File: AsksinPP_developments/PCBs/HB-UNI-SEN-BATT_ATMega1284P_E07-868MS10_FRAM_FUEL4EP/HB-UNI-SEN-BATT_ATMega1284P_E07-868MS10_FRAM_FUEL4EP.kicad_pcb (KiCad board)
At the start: 2 copper layers, 75 x 75 mm, 63 parts, among them J1 Conn_01x02, J10 charge, J11 ePaper connector, J12 FTDI Debuger, J13 BME680, J2 Conn_01x02, J3 Conn_01x02, J4 Conn_01x02, J5 ISP Programmer, J6 SHT85, J7 AHT25, J8 AHT20+BMP280, J9 BME280/BMP280, Q1 IRLU024N, SW1 Config button, SW2 Reset button, U1 ATmega1284P-AU, U2 TPS61221DCK, U3 MB85RS2MTPF, U4 MB85RS2MTPF, Y1 8MHz

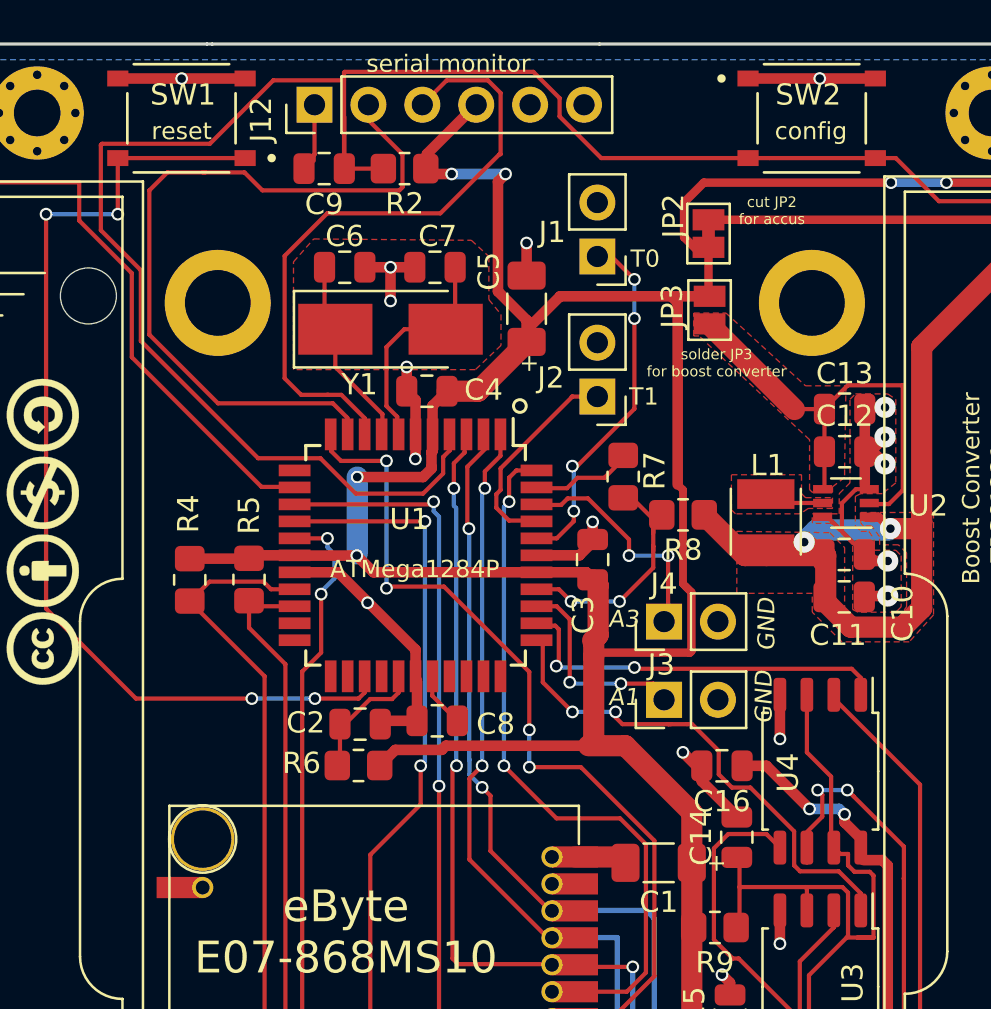
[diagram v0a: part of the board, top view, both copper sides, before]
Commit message: PCBs/HB-UNI-SEN-BATT_ATMega1284P_E07-868MS10_FUEL4EP and PCBs/HB-UNI-SEN-BATT_ATMega1284P_E07-868MS10_FRAM_FUEL4EP: changed R8 from 200kOhm to 47kOhm for better measurement accuracy
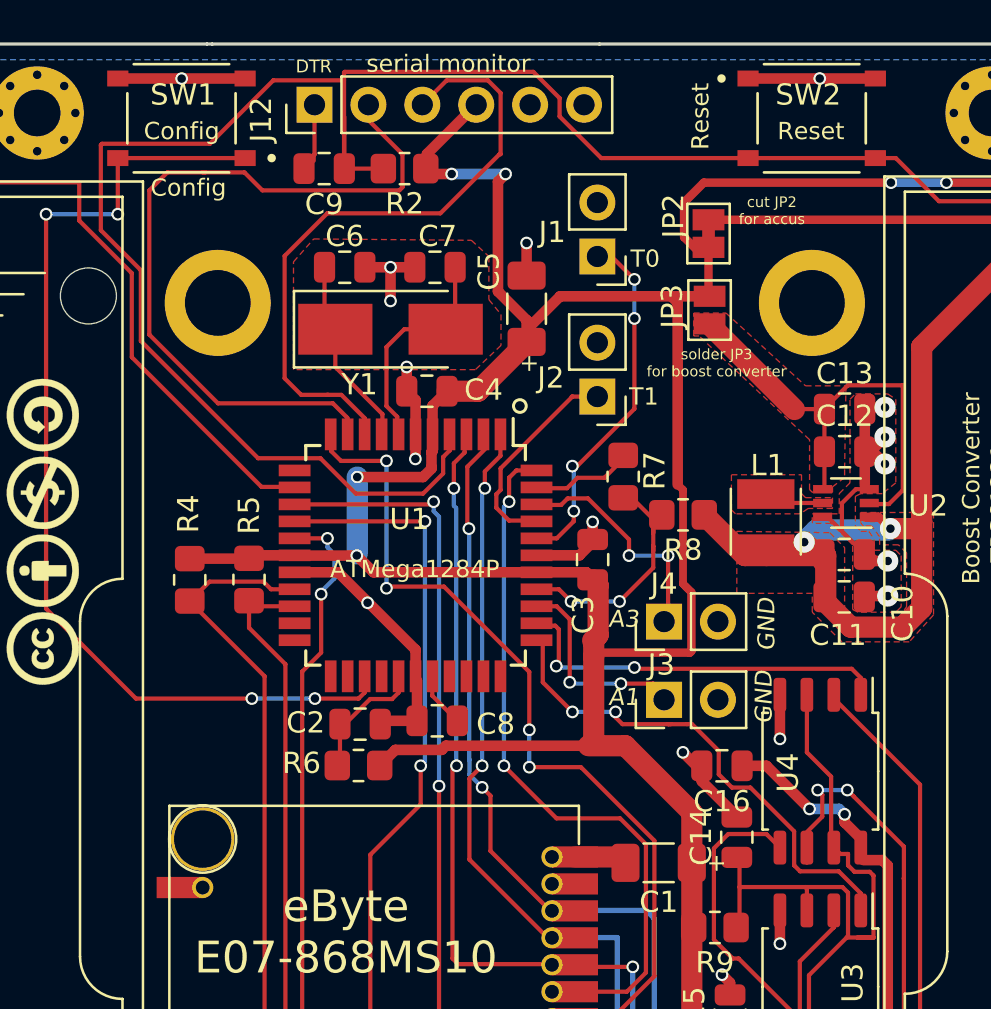
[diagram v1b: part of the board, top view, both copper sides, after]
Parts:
- R8: value 200k -> 47k
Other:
- board text added: "Config"
- board text added: "DTR"
- board text added: "Reset"
- board text added: "Version 1.1 - 01/2022"
- board text removed: "Version 1.0 - 11/2021"
- board text removed: "config"
- board text removed: "reset"

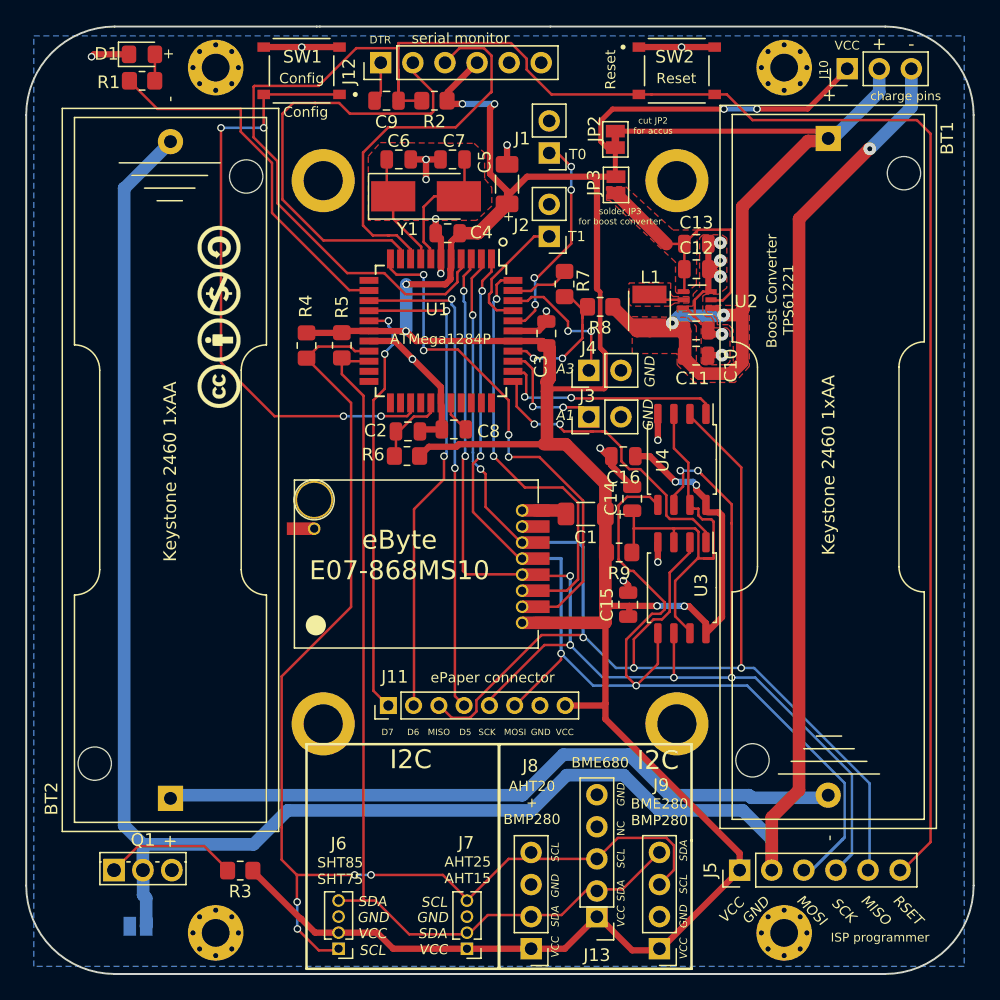
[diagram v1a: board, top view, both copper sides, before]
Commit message: major update: hb-ep-devices-addon V1.14; added sketches HB-UNI-Sensor1-AQ-BME680_KF_rLF and HB-UNI-SenAct-4-4-SC_DS; migration of all PPCBs to KiCAD 6
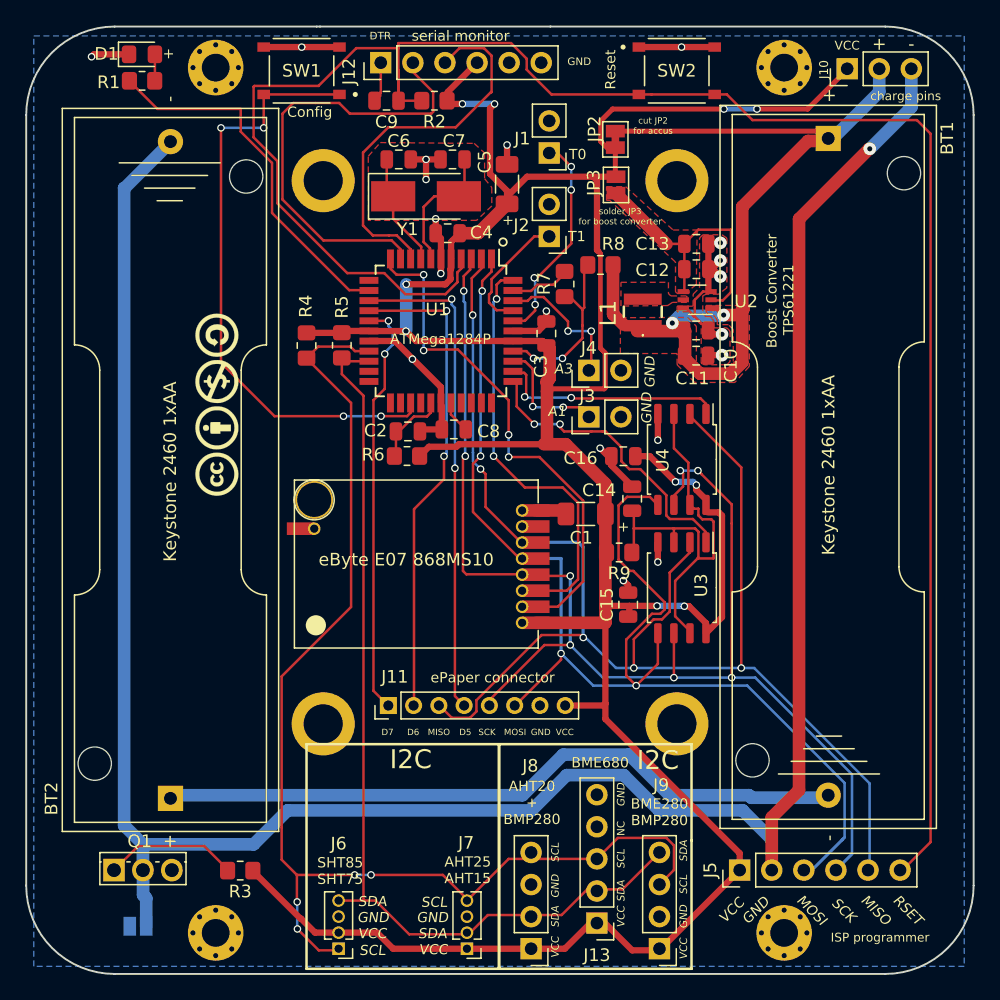
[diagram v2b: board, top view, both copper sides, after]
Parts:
- L1: footprint FUEL4EP:Fastron L-1212FPS 4.7uH SMD Inductor -> FUEL4EP:FUEL4EP_Inductor_SMD_1
- moved LOGO1 6.95 mm to (116.1, 108.0)
- moved R8 3.31 mm to (146.5, 96.9)
- moved L1 1.79 mm to (149.8, 100.6)
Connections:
- net /~hold renamed /~{hold}
- J13 pad 4: Net-(J13-Pad4) -> unconnected-(J13-Pad4)
- Module1 pad 2A: Net-(Module1-Pad2A) -> unconnected-(Module1-Pad2A)
- Module1 pad 7C: Net-(Module1-Pad7C) -> unconnected-(Module1-Pad7C)
- U1 pad 12: Net-(U1-Pad12) -> unconnected-(U1-Pad12)
- U1 pad 21: Net-(U1-Pad21) -> unconnected-(U1-Pad21)
- U1 pad 22: Net-(U1-Pad22) -> unconnected-(U1-Pad22)
- U1 pad 23: Net-(U1-Pad23) -> unconnected-(U1-Pad23)
- U1 pad 24: Net-(U1-Pad24) -> unconnected-(U1-Pad24)
- U1 pad 26: Net-(U1-Pad26) -> unconnected-(U1-Pad26)
- U1 pad 30: Net-(U1-Pad30) -> unconnected-(U1-Pad30)
- U1 pad 31: Net-(U1-Pad31) -> unconnected-(U1-Pad31)
- U1 pad 32: Net-(U1-Pad32) -> unconnected-(U1-Pad32)
- U1 pad 33: Net-(U1-Pad33) -> unconnected-(U1-Pad33)
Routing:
- net VCC: track 254.6 -> 251.4 mm
- net Net-(L1-Pad2): track 2.67 -> 0.00 mm
- net /plusBAT: track 69.9 -> 72.4 mm
- net /A0: track 12.1 -> 14.0 mm
- net /PA3: track 24.3 -> 22.9 mm
- net /~{hold}: track 33.1 -> 32.4 mm
- net /minusBAT: track 189.6 -> 189.0 mm
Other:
- net class Default removed
- net class battery removed
- net class supply removed
- board text added: "Version 1.2 - 07/2023 (KiCAD 6)"
- board text removed: "Version 1.1 - 01/2022"
- board text removed: "eByte E07-868MS10"

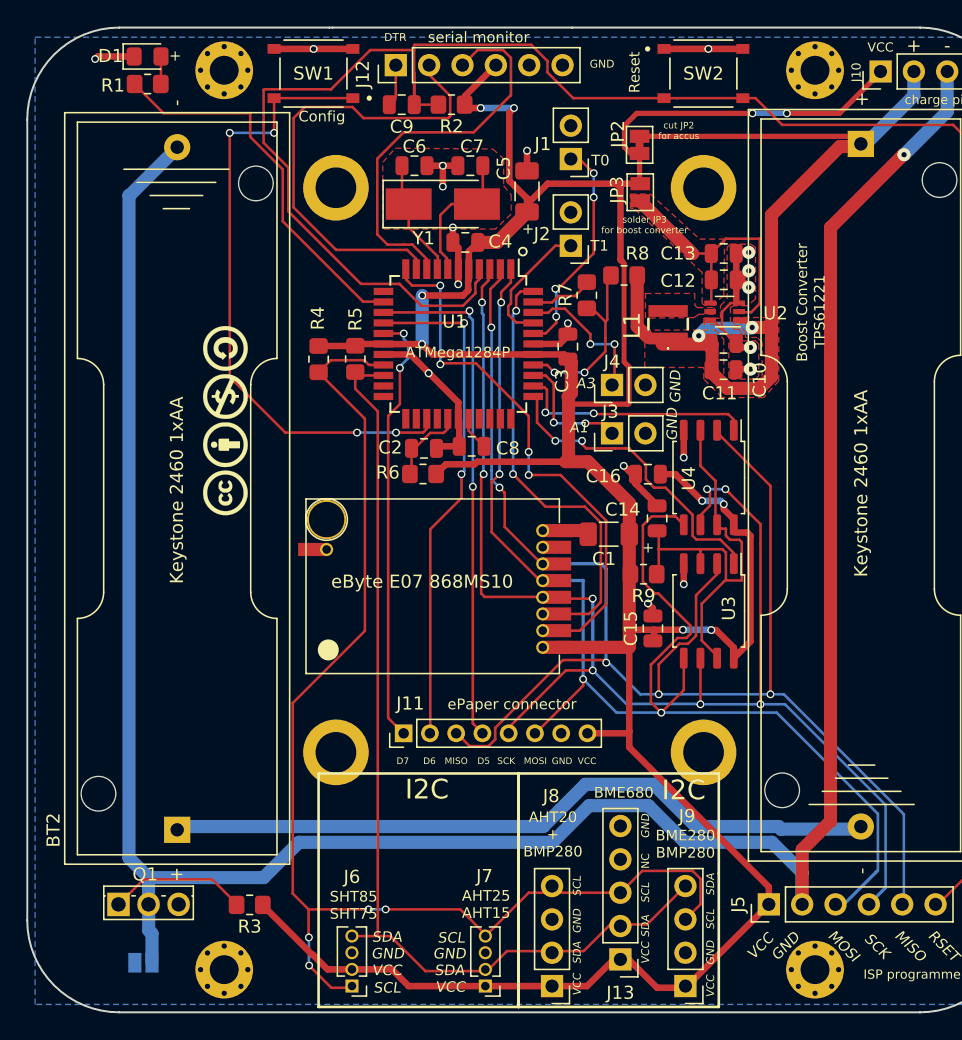
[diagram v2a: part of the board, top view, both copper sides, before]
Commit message: PCBs: KiCAD6 required improvements of layout data bases; added E07-900M10S into FUEL and footprint library
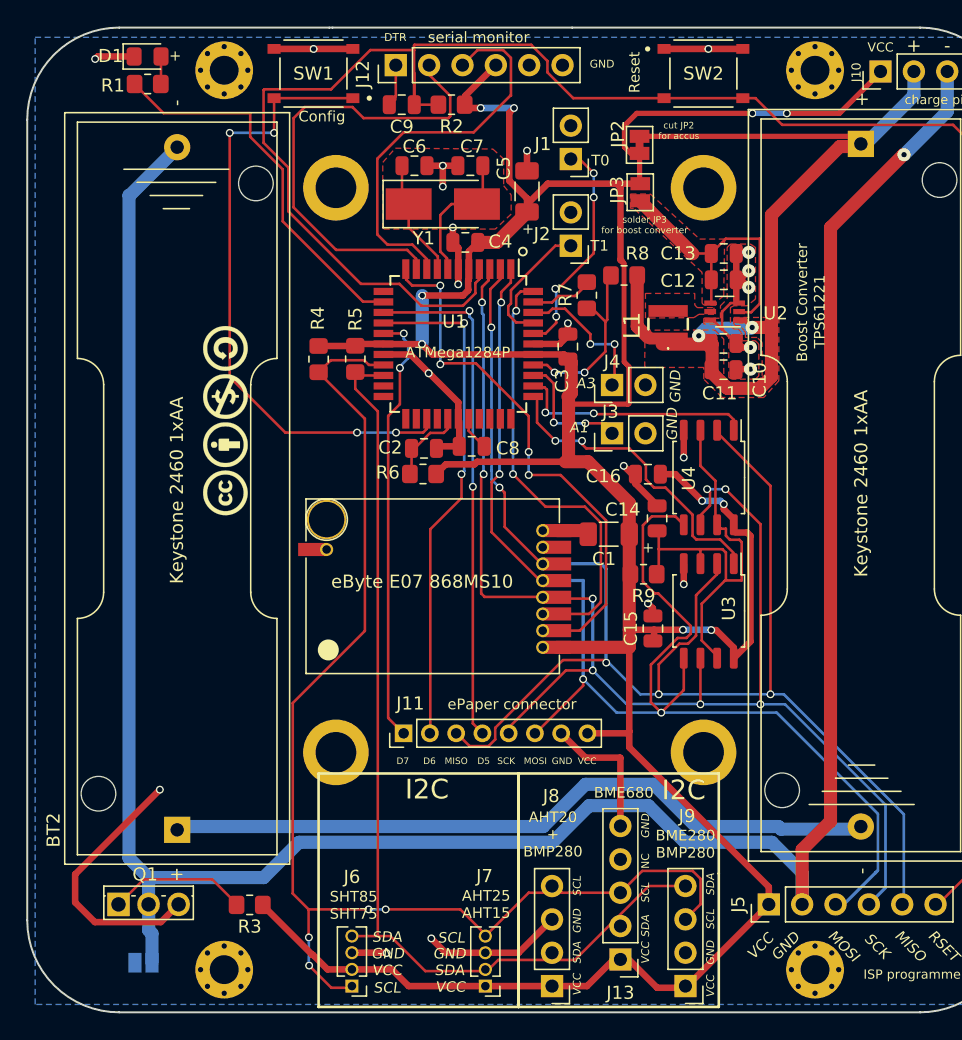
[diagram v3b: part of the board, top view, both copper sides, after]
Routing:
- net GND: track 65.9 -> 109.6 mm, vias 19 -> 22
- net /PB0_T0: track 17.8 -> 16.5 mm
- net /plusBAT: track 72.4 -> 71.6 mm
- net /Vout: track 21.6 -> 20.8 mm
- net VCC: track 251.4 -> 250.6 mm
- net /TXD0: track 35.8 -> 35.0 mm
- net /conBAT: track 55.3 -> 54.6 mm
- net /MOSI: track 105.4 -> 104.8 mm
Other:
- board text added: "Version 1.3 - 07/2023 (KiCAD 6)"
- board text removed: "Version 1.2 - 07/2023 (KiCAD 6)"
